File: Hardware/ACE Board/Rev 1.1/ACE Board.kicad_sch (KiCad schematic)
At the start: 188 parts, among them J1 PHI2 SELECT, J10 PORT A, J11 AUDIO L, J12 DB9 MALE (DTE), J13 PS/2, J14 KEYBOARD, J15 AUDIO R, J16 AUDIO, J17 5V DC, J18 CART, J19 BUS, J2 CTS EN, J20 VCC, J21 POWER LED, J22 STORAGE, J3 RESET SW, J4 DCD EN, J5 VDD, J6 JOYSTICK A, J7 PADDLES, J8 JOYSTICK B, J9 PORT B, SW1 `, SW10 9, SW11 0, SW12 -, SW13 =, SW14 BACKSPACE, SW15 ESCAPE, SW16 TAB, SW17 RESET, SW18 Q, SW19 W, SW2 1, SW20 E, SW21 R, SW22 T, SW23 Y, SW24 U, SW25 I, SW26 O, SW27 P, SW28 [, SW29 ], SW3 2, SW30 \, SW31 INSERT, SW32 CAPS LOCK, SW33 A, SW34 S, SW35 D, SW36 F, SW37 G, SW38 H, SW39 J, SW4 3, SW40 K, SW41 L, SW42 SHIFT, SW43 ;, SW44 ', SW45 ENTER, SW46 DELETE, SW47 Z, SW48 X, SW49 C, SW5 4, SW50 SHIFT, SW51 V, SW52 B, SW53 N, SW54 M, SW55 ,, SW56 ., SW57 /, SW58 UP ARROW, SW59 CTRL, SW6 5, SW60 ALT, SW61 MENU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

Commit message: Fix the bank register decode, and run the ACE at 1 MHz only
The bank latches loaded on 259 addresses each, not just $83FF and $87FF:
U12B NANDed two active-low terms, which ORs them, so a write anywhere in
$8300-$83FF or to $80FF-$82FF (and the same at $8400) changed the bank.
Rev 1.0, Rev 1.1 as drawn and the first RAM Patch all had it.

- Rev 1.1: a spare NOR (U23C) takes U12B's place.
- ACE RAM Patch Rev 1.1: plugs into U12's and U13's sockets, since A8, A9
  and U17's output never reach U13's, and replaces both 74HC00s.
- Rev 1.1 runs at 1 MHz only. J1 is gone and U5's Q3 clocks the CPU, VIA,
  ACIA and SID. At 2 MHz the SID, always on the 1 MHz tap, answered only
  every other cycle, and a serial fault under BIOS 1.6 went unexplained.
- Rev 1.1 gets D4 on the video card's /INT and R35 pulling up RESB
  (TODO items 1 and 2).
- Tests/check-schematics.mjs evaluates both boards' decode from their
  netlists in all 524,288 bus states, and checks the clock, the /INT diode
  and the RESB pull-up. It fails on every earlier version of the latch.

Co-Authored-By: Claude Opus 5.5 (1M context) <noreply@anthropic.com>
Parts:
- removed J1: PHI2 SELECT, Connector_PinHeader_2.54mm:PinHeader_1x03_P2.54mm_Vertical, symbol Connector_Generic:Conn_01x03
- added D4: BAT85, Diode_THT:D_DO-35_SOD27_P7.62mm_Horizontal, symbol Device:D_Schottky
- added R35: 10k, Resistor_THT:R_Axial_DIN0204_L3.6mm_D1.6mm_P5.08mm_Horizontal, symbol Device:R
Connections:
- net PHI2_1MHZ is gone; now on net PHI2: U5.11 (Q3), U9.6 (PHI2)
- net GND: now also U12.4, U12.5; no longer U23.8, U23.9
- net IRQB: now also D4.2 (A); no longer U3.16 (~{INT})
- net RESB: now also R35.1
- net VCC: now also R35.2
- net at U12.3: now also U23.8; no longer U12.4
- net at U13.1, U13.4: now also U23.10; no longer U12.6
- net at U17.8: now also U23.9; no longer U12.5
- net PHI2_2MHZ: no longer names the net of U5.12 (Q2)
- new net: D4.1 (K), U3.16 (~{INT})
- no-connect marks 36 -> 37
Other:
- moved on the sheet: U12B, U23C, U3

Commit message: ACE Board Rev 1.1: the bank latch on two chips, re-annotated, PCB done
- The latch logic uses eight gates on U12 (74HC00) and U13 (74HC02), the same
  gates as the ACE RAM Patch Rev 1.1. The IO1 inverter is a NOR now, which
  frees a whole 74HC00: Rev 1.0's second 74HC00 is gone.
- Re-annotated: J2-J22 are J1-J21, D1-D3 are D2-D4, R5-R34 are R6-R35,
  C20-C30 are C21-C31, the bulk capacitor is C20, the /INT diode D1, the
  RESB pull-up R5, and the 74HC02 U13.
- The PCB is updated from the schematic with every placed part where it
  was: no DRC errors, nothing unconnected, no schematic parity issues.
  Production files, the 3D model and the renders are regenerated.
- Tests/check-schematics.mjs names the parts it reads and checks their
  values, so a re-annotation fails loudly instead of checking the wrong chip.
- The AB Controller README gives Rev 1.1's joystick designators.

Co-Authored-By: Claude Opus 5.5 (1M context) <noreply@anthropic.com>
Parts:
- removed U13: 74HC00, Package_DIP:DIP-14_W7.62mm_Socket_LongPads, symbol 74xx:74HC00
- renumbered C31 to C20, C20 to C21, C21 to C22, C22 to C23, C23 to C24, C24 to C25, C25 to C26, C26 to C27, C27 to C28, C28 to C29, C29 to C30, C30 to C31, D4 to D1, D1 to D2, D2 to D3, D3 to D4, J2 to J1, J11 to J10, J12 to J11, J13 to J12, J14 to J13, J15 to J14, J16 to J15, J17 to J16, J18 to J17, J19 to J18, J20 to J19, J3 to J2, J21 to J20, J22 to J21, J4 to J3, J5 to J4, J6 to J5, J7 to J6, J8 to J7, J9 to J8, J10 to J9, R9 to R10, R10 to R11, R11 to R12, R12 to R13, R13 to R14, R14 to R15, R15 to R16, R16 to R17, R17 to R18, R18 to R19, R19 to R20, R20 to R21, R21 to R22, R22 to R23, R23 to R24, R24 to R25, R25 to R26, R26 to R27, R27 to R28, R28 to R29, R29 to R30, R30 to R31, R31 to R32, R32 to R33, R33 to R34, R34 to R35, R35 to R5, R5 to R6, R6 to R7, R7 to R8, R8 to R9, U23 to U13
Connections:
- net B18: now also U12.10
- net GND: no longer U12.4, U12.5, U13.11, U13.12
- net IO1B: now also U13.11, U13.12; no longer U12.10, U12.9
- net at U13.10: now also U12.4, U12.9
- net at U13.5: now also U12.8
- net at U13.2: now also U12.6
- net at U13.13: now also U12.5
- no-connect marks 37 -> 33
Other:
- moved on the sheet: U12B, U12C, U13D, U13E, U17B

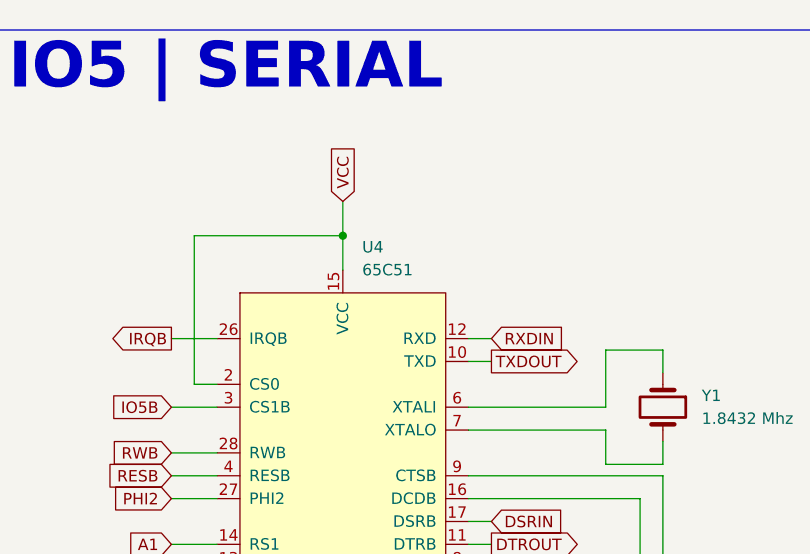
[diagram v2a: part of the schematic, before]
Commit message: ACE Board Rev 1.1: name the ACIA as the R6551AP
U4's value field names the part tested on the AC6502 machines, the
R6551AP, where it said only "65C51". It changes in the schematic and on
the PCB, where the value sits on the silkscreen inside U4's socket
outline. The README's feature list and BOM say the same, and the
schematic PDF is plotted again. Rev 1.1 is unproduced; its production
files are regenerated with P1.7's 1N5819.

Rev 1.0 was fabricated and keeps "65C51". So the checker's parts table
now takes a value per revision (a config's `values`), and passes for
both revisions.

Co-Authored-By: Claude Opus 5.5 <noreply@anthropic.com>
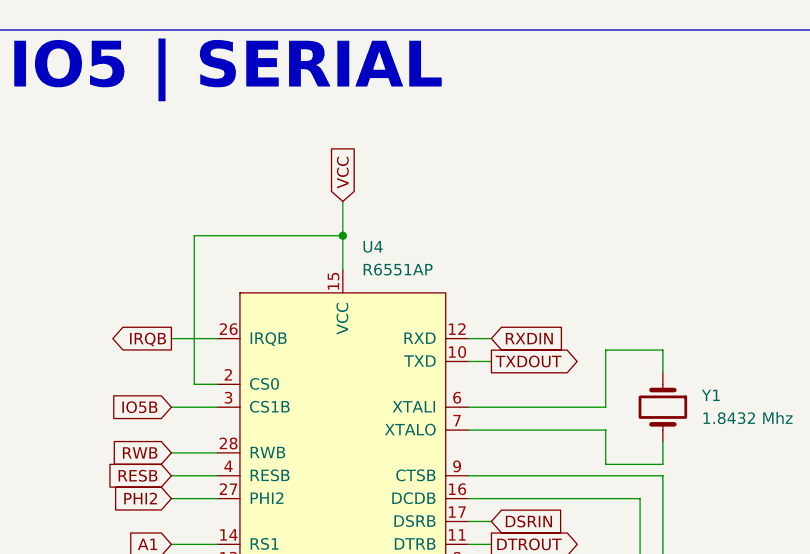
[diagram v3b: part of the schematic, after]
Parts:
- U4: value 65C51 -> R6551AP
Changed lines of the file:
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@@
 			)
 		)
-		(property "Value" "65C51"
+		(property "Value" "R6551AP"
 			(at 513.9533 40.64 0)
 			(show_name no)

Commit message: ACE Board Rev 1.1: reverse-polarity protection on the barrel jack
D5, a 1N5819 (DO-41), in series between the barrel jack (J16) and the
power switch (SW69), anode at the jack: the same part and place as on the
KIM Board. Rev 1.1 has not been produced, so the fix goes into it.

The netlist differs from before only there: J16 pin 1 -> D5 -> SW69 pin 2.
ERC and DRC are clean, nothing is unconnected, and check-schematics.mjs
passes. The production files, schematic PDF, renders and STEP model are
regenerated. The remaining silkscreen clearance warnings, which predate
this change, are excluded in the project.

The diode drops about 0.3-0.4 V, so VCC sits near 4.6 V; measure it under
full load on the first board built.

Co-Authored-By: Claude Opus 5.5 <noreply@anthropic.com>
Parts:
- added D5: 1N5819, Diode_THT:D_DO-41_SOD81_P10.16mm_Horizontal, symbol Device:D_Schottky
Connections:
- net at SW69.2 (B): now also D5.1 (K); no longer J16.1
- new net: D5.2 (A), J16.1
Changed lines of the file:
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@@
 	(wire
 		(pts
-			(xy 600.71 252.73) (xy 609.6 252.73)
+			(xy 608.33 252.73) (xy 609.6 252.73)
 		)
 		(stroke
@@
 					(unit 1)
 				)
+			)
+		)
+	)
+	(symbol
+		(lib_id "Device:D_Schottky")
+		(at 604.52 252.73 180)
+		(unit 1)
+		(body_style 1)
+		(exclude_from_sim no)
+		(in_bom yes)
+		(on_board yes)
+		(in_pos_files yes)
+		(dnp no)
+		(property "Reference" "D5"
+			(at 604.52 247.65 0)
+			(show_name no)
+			(do_not_autoplace no)
+			(effects
+				(font
+					(size 1.27 1.27)
+				)
+			)
+		)
+		(property "Value" "1N5819"
+			(at 604.774 249.682 0)
+			(show_name no)
+			(do_not_autoplace no)
+			(effects
+				(font
+					(size 1.27 1.27)
+				)
+			)
+		)
+		(property "Footprint" "Diode_THT:D_DO-41_SOD81_P10.16mm_Horizontal"
+			(at 604.52 252.73 0)
+			(hide yes)
+			(show_name no)
+			(do_not_autoplace no)
+			(effects
+				(font
+					(size 1.27 1.27)
+				)
+			)
+		)
+		(property "Datasheet" ""
+			(at 604.52 252.73 0)
+			(hide yes)
+			(show_name no)
+			(do_not_autoplace no)
+			(effects
+				(font
+					(size 1.27 1.27)
+				)
+			)
+		)
+		(property "Description" "Schottky diode"
+			(at 604.52 252.73 0)
+			(hide yes)
+			(show_name no)
+			(do_not_autoplace no)
+			(effects
+				(font
+					(size 1.27 1.27)
+				)
+			)
+		)
+		(pin "2"
+		)
+		(pin "1"
+		)
+		(instances
+			(project "ACE Board"
+				(path "/34a60d42-c14a-479d-bef3-5ff0ee57bad5"
+					(reference "D5")
+					(unit 1)
+				)
